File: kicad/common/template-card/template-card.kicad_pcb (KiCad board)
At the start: 2 copper layers, 38 x 64 mm, 18 parts, among them J1 Conn_01x06_Pin, J2 Conn_01x06_Pin, J4 Conn_01x05, U1 THVD1450DR, U2 STM32C011F4Px

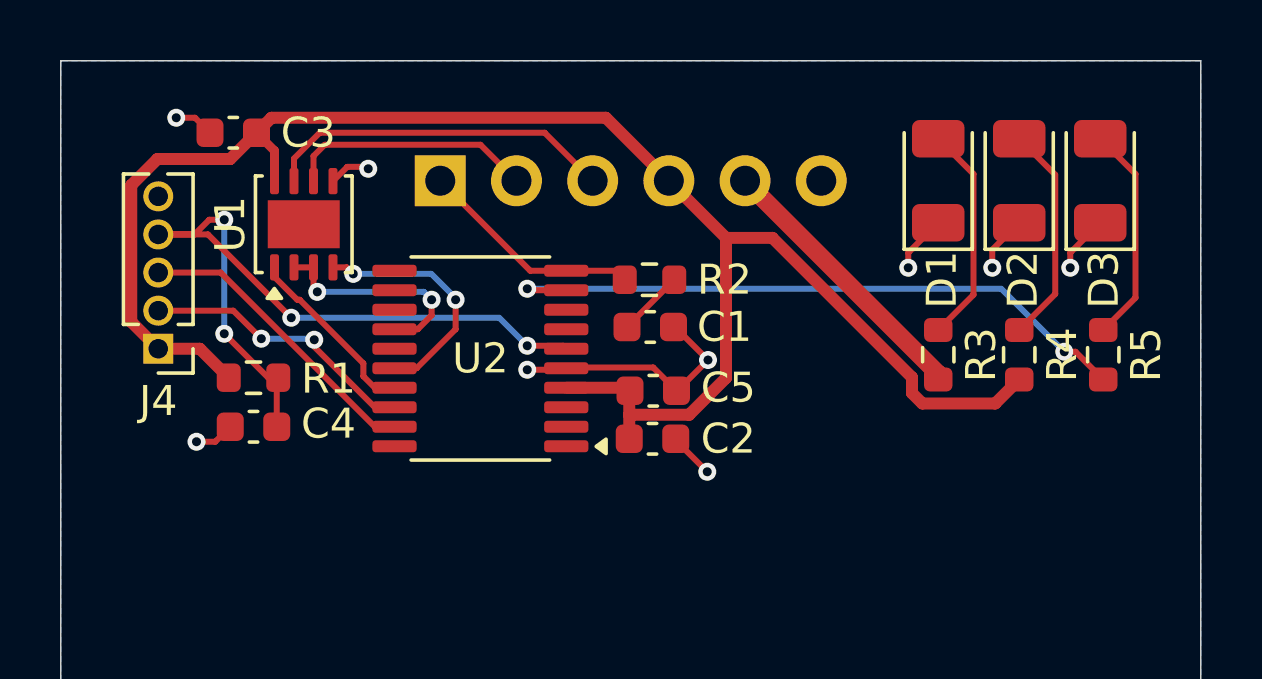
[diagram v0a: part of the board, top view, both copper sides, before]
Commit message: Update card template and MIDI Buddy
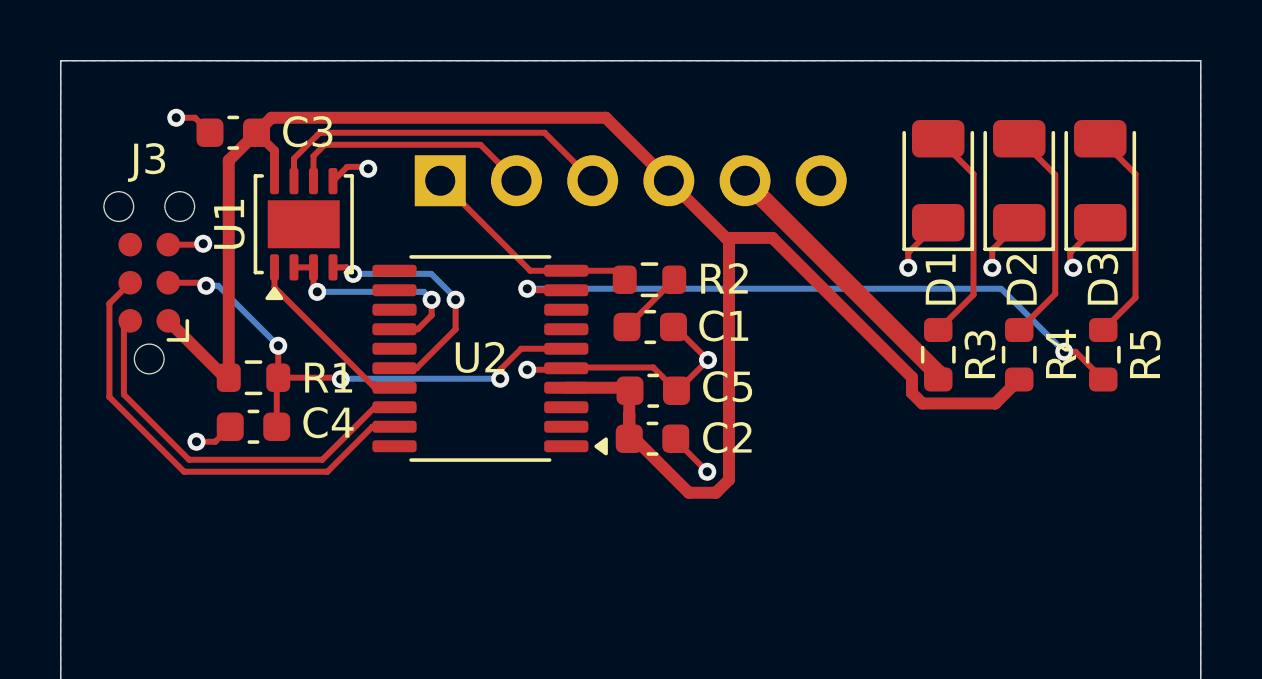
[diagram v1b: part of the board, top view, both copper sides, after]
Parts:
- removed J4: Conn_01x05, Connector_PinHeader_1.27mm:PinHeader_1x05_P1.27mm_Vertical
- added J3: Conn_ARM_SWD_TagConnect_TC2030-NL, Connector:Tag-Connect_TC2030-IDC-NL_2x03_P1.27mm_Vertical, F.Cu at (125.2, 60.9)
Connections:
- J1 pad 1: SLOT -> MCLK
- J1 pad 2: BUS A -> BLCK
- J1 pad 3: BUS B -> FSYNC
- J1 pad 4: +3V3 -> S4_AUDIO_IN
- J1 pad 5: +5V -> S4_AUDIO_OUT
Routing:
- net NRST: track 25.4 -> 17.5 mm
- net SWCLK: track 10.0 -> 15.3 mm
- net SWDIO: track 9.34 -> 13.2 mm, vias 2 -> 0
- net +3V3: track 57.7 -> 60.2 mm
- net GND: track 19.7 -> 20.9 mm, vias 9 -> 10
